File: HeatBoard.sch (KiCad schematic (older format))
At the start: 19 parts, among them J81 J8HeaderTurned, J82 J8Header, Q1 BC337, Q2 BC337

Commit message: First Final
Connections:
- net at Bu1.1 (V+), Co2.1 (P1), Co3.1 (P1)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: no longer R2.1 (P1)
- net at Co1.1 (P1), J81.1 (3.3V), J82.1 (3.3V)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: now also R2.1 (P1)
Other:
- moved on the sheet: Co2, Q1, R2, R3
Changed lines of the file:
@@
 L BC337 Q1
 U 1 1 5BE89444
-P 10050 3200
-F 0 "Q1" H 10250 3275 50  0000 L CNN
-F 1 "BC337" H 10250 3200 50  0000 L CNN
-F 2 "RasperryLib:BC337" H 10250 3125 50  0001 L CIN
-F 3 "" H 10050 3200 50  0001 L CNN
-	1    10050 3200
+P 10550 3200
+F 0 "Q1" H 10750 3275 50  0000 L CNN
+F 1 "BC337" H 10750 3200 50  0000 L CNN
+F 2 "RasperryLib:BC337" H 10750 3125 50  0001 L CIN
+F 3 "" H 10550 3200 50  0001 L CNN
+	1    10550 3200
 	1    0    0    -1
 $EndComp
@@
 L Conn_small1x3 Co2
 U 1 1 5BE8BABB
-P 6800 5950
-F 0 "Co2" H 6800 5700 60  0000 C CNN
-F 1 "DHT22" H 6800 6150 60  0000 C CNN
-F 2 "RasperryLib:Conn_Small1x3" H 6800 5950 60  0001 C CNN
-F 3 "" H 6800 5950 60  0001 C CNN
-	1    6800 5950
+P 7050 5950
+F 0 "Co2" H 7050 5700 60  0000 C CNN
+F 1 "DHT22" H 7050 6150 60  0000 C CNN
+F 2 "RasperryLib:Conn_Small1x3" H 7050 5950 60  0001 C CNN
+F 3 "" H 7050 5950 60  0001 C CNN
+	1    7050 5950
 	1    0    0    -1
 $EndComp
@@
 L Resistor R2
 U 1 1 5BE8E5B2
-P 6800 5200
-F 0 "R2" H 6800 5100 60  0000 C CNN
-F 1 "10k" H 6800 5300 60  0000 C CNN
-F 2 "RasperryLib:Resistor" H 6800 5200 60  0001 C CNN
-F 3 "" H 6800 5200 60  0001 C CNN
-	1    6800 5200
-	0    1    1    0
+P 6250 5950
+F 0 "R2" H 6250 5850 60  0000 C CNN
+F 1 "10k" H 6250 6050 60  0000 C CNN
+F 2 "RasperryLib:Resistor" H 6250 5950 60  0001 C CNN
+F 3 "" H 6250 5950 60  0001 C CNN
+	1    6250 5950
+	1    0    0    -1
 $EndComp
 $Comp
@@
 L Resistor R3
 U 1 1 5BE90BEE
-P 9650 3050
-F 0 "R3" H 9650 2950 60  0000 C CNN
-F 1 "1k" H 9650 3150 60  0000 C CNN
-F 2 "RasperryLib:Resistor" H 9650 3050 60  0001 C CNN
-F 3 "" H 9650 3050 60  0001 C CNN
-	1    9650 3050
-	0    1    1    0
+P 10100 3200
+F 0 "R3" H 10100 3100 60  0000 C CNN
+F 1 "1k" H 10100 3300 60  0000 C CNN
+F 2 "RasperryLib:Resistor" H 10100 3200 60  0001 C CNN
+F 3 "" H 10100 3200 60  0001 C CNN
+	1    10100 3200
+	1    0    0    -1
 $EndComp
 $Comp
@@
 	0    1    1    0
 $EndComp
+$Comp
+L Buzzer_2 Bu1
+U 1 1 5BE9F2D6
+P 8100 5050
+F 0 "Bu1" H 8100 4750 60  0000 C CNN
+F 1 "Buzzer_2" H 8100 5350 60  0000 C CNN
+F 2 "RasperryLib:Buzzer1x2" H 8100 4850 60  0001 C CNN
+F 3 "" H 8100 4850 60  0001 C CNN
+	1    8100 5050
+	1    0    0    -1
+$EndComp
+$Comp
+L BC337 Q2
+U 1 1 5BE9F3DC
+P 8000 5550
+F 0 "Q2" H 8200 5625 50  0000 L CNN
+F 1 "BC337" H 8200 5550 50  0000 L CNN
+F 2 "TO_SOT_Packages_THT:TO-92_Molded_Narrow" H 8200 5475 50  0001 L CIN
+F 3 "" H 8000 5550 50  0001 L CNN
+	1    8000 5550
+	1    0    0    -1
+$EndComp
+$Comp
+L Resistor R4
+U 1 1 5BE9F598
+P 7800 5250
+F 0 "R4" H 7800 5150 60  0000 C CNN
+F 1 "1k" H 7800 5350 60  0000 C CNN
+F 2 "RasperryLib:Resistor" H 7800 5250 60  0001 C CNN
+F 3 "" H 7800 5250 60  0001 C CNN
+	1    7800 5250
+	0    1    1    0
+$EndComp
 Wire Wire Line
 	4200 3850 4550 3850
@@
 	6150 5450 6150 5500
 Wire Wire Line
-	6550 5500 2600 5500
+	2600 5500 6550 5500
 Wire Wire Line
 	2600 5500 2600 5450
@@
 	9300 4250 7150 4250
 Wire Wire Line
-	7150 4250 7150 4050
-Wire Wire Line
-	7150 4050 6150 4050
+	7150 4050 7150 5850
+Wire Wire Line
+	6150 4050 7150 4050
 Wire Wire Line
 	9150 3550 9150 3850
 Connection ~ 10150 3750
-Wire Wire Line
-	10800 3000 10150 3000
 Connection ~ 10800 3750
 Wire Wire Line
-	10150 3400 9450 3400
-Wire Wire Line
 	9450 3400 9450 3850
 Wire Wire Line
-	6700 3850 6700 5850
-Connection ~ 6700 3850
-Wire Wire Line
-	6900 5850 6900 4050
-Connection ~ 6900 4050
+	6950 3850 6950 5850
+Connection ~ 6950 3850
+Connection ~ 7150 4050
 Wire Wire Line
 	7400 5850 7400 3850
@@
 Connection ~ 7600 4250
 Wire Wire Line
-	6800 5000 6700 5000
-Connection ~ 6700 5000
-Wire Wire Line
-	6800 5400 6800 5850
+	6800 5550 6800 5950
+Wire Wire Line
+	6800 5850 7050 5850
 Wire Wire Line
 	6150 5550 6800 5550
@@
 Connection ~ 4450 5650
 Wire Wire Line
-	4350 5950 4100 5950
+	4100 5950 6050 5950
 Connection ~ 4350 5950
 Wire Wire Line
 	4100 6350 4450 6350
 Connection ~ 4450 6350
-Wire Wire Line
-	6150 5750 6350 5750
-Wire Wire Line
-	9650 3250 9850 3250
-Wire Wire Line
-	9850 3250 9850 3200
 Connection ~ 9450 3550
-$Comp
-L Buzzer_2 Bu1
-U 1 1 5BE9F2D6
-P 8100 5050
-F 0 "Bu1" H 8100 4750 60  0000 C CNN
-F 1 "Buzzer_2" H 8100 5350 60  0000 C CNN
-F 2 "RasperryLib:Buzzer1x2" H 8100 4850 60  0001 C CNN
-F 3 "" H 8100 4850 60  0001 C CNN
-	1    8100 5050
-	1    0    0    -1
-$EndComp
 Wire Wire Line
 	8100 4850 8100 3850
 Connection ~ 8100 3850
-$Comp
-L BC337 Q2
-U 1 1 5BE9F3DC
-P 8000 5550
-F 0 "Q2" H 8200 5625 50  0000 L CNN
-F 1 "BC337" H 8200 5550 50  0000 L CNN
-F 2 "TO_SOT_Packages_THT:TO-92_Molded_Narrow" H 8200 5475 50  0001 L CIN
-F 3 "" H 8000 5550 50  0001 L CNN
-	1    8000 5550
-	1    0    0    -1
-$EndComp
 Wire Wire Line
 	8100 5250 8100 5350
@@
 	8350 5750 8350 4250
 Connection ~ 8350 4250
-$Comp
-L Resistor R4
-U 1 1 5BE9F598
-P 7800 5250
-F 0 "R4" H 7800 5150 60  0000 C CNN
-F 1 "1k" H 7800 5350 60  0000 C CNN
-F 2 "RasperryLib:Resistor" H 7800 5250 60  0001 C CNN
-F 3 "" H 7800 5250 60  0001 C CNN
-	1    7800 5250
-	0    1    1    0
-$EndComp
 Wire Wire Line
 	7800 5450 7800 5550
@@
 	6600 6250 6600 4050
 Connection ~ 6600 4050
-Wire Wire Line
-	6550 2850 6550 5500
-Wire Wire Line
-	6550 2850 9650 2850
 Connection ~ 6150 5500
+Connection ~ 6800 5850
+Wire Wire Line
+	6800 5950 6450 5950
+Connection ~ 7150 4250
+Wire Wire Line
+	6550 5500 6550 3200
+Wire Wire Line
+	6550 3200 9900 3200
+Wire Wire Line
+	10300 3200 10350 3200
+Wire Wire Line
+	10650 3400 9450 3400
+Wire Wire Line
+	10800 3000 10650 3000
 $EndSCHEMATC

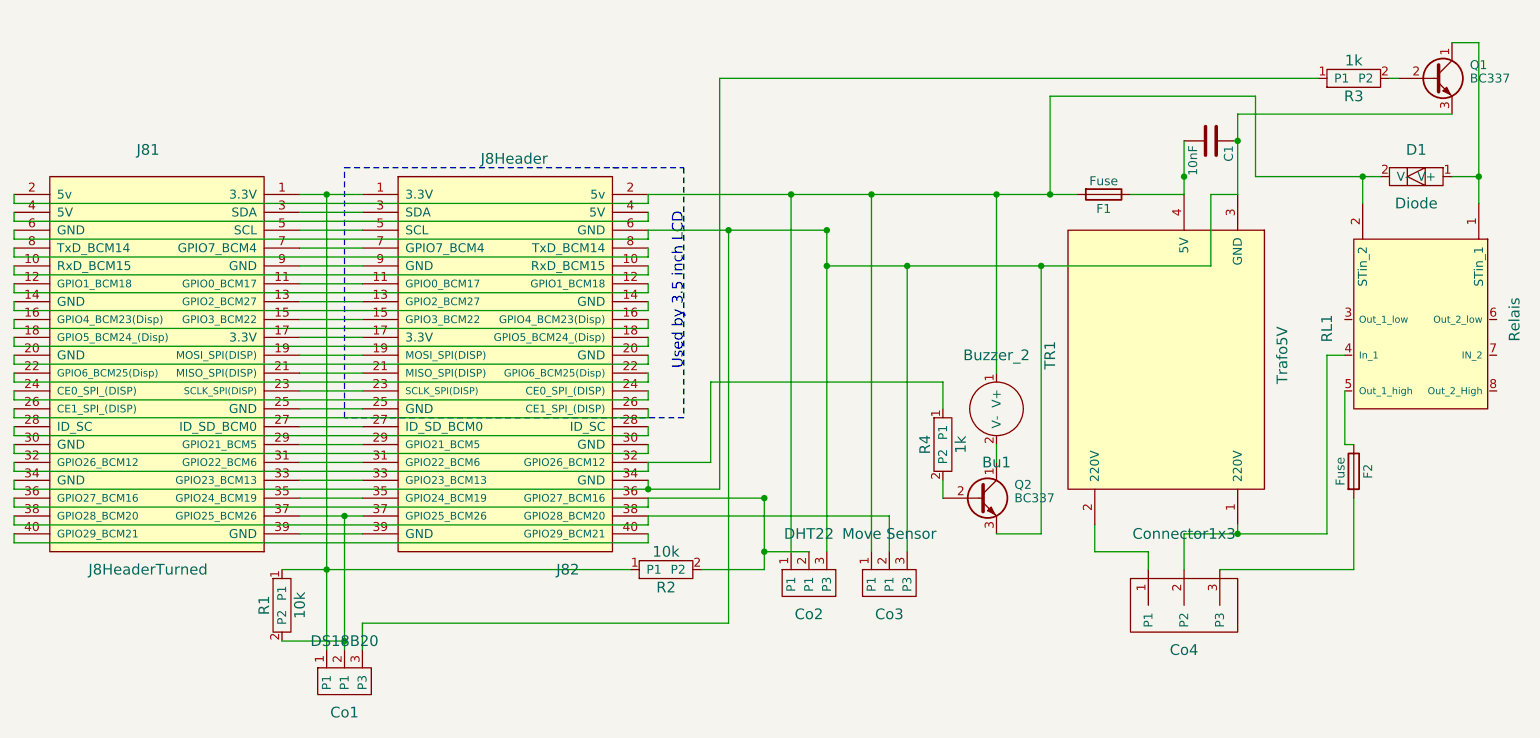
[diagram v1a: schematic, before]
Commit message: Raspi Connections move, GND Pin free now
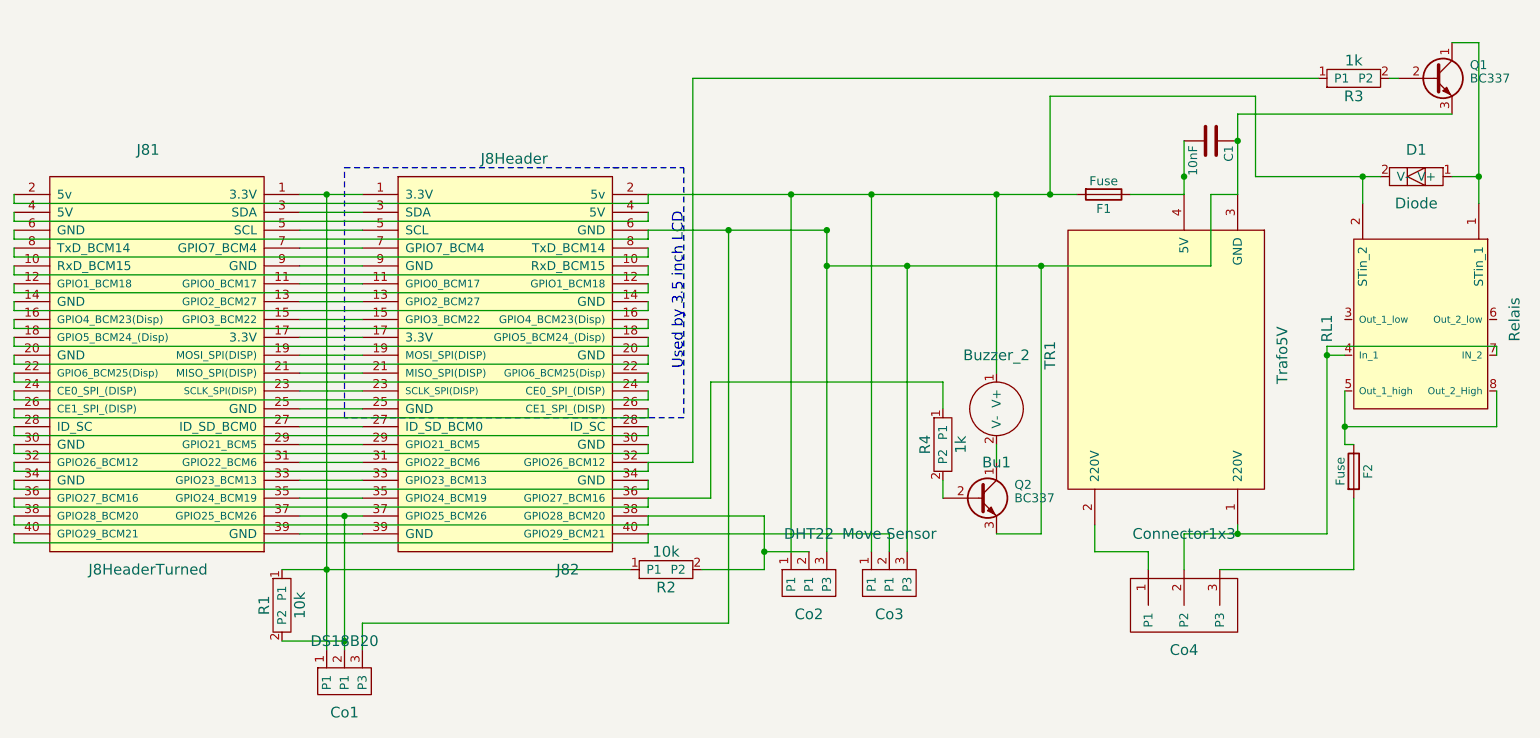
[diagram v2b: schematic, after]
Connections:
- net at Co4.2 (P2), RL1.4 (In_1), TR1.1 (220V): now also RL1.7 (IN_2)
- net at F2.1, RL1.5 (Out_1_high): now also RL1.8 (Out_2_High)
- net at J81.32 (GPIO26_BCM12), J82.32 (GPIO26_BCM12): now also R3.1 (P1); no longer R4.1 (P1)
- net at J81.34 (GND), J82.34 (GND): no longer R3.1 (P1)
- net at J81.36 (GPIO27_BCM16), J82.36 (GPIO27_BCM16): now also R4.1 (P1); no longer Co2.2 (P1), R2.2 (P2)
- net at J81.38 (GPIO28_BCM20), J82.38 (GPIO28_BCM20): now also Co2.2 (P1), R2.2 (P2); no longer Co3.2 (P1)
- net at J81.40 (GPIO29_BCM21), J82.40 (GPIO29_BCM21): now also Co3.2 (P1)
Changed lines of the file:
@@
 	6150 5450 6150 5500
 Wire Wire Line
-	2600 5500 6550 5500
+	6150 5500 2600 5500
 Wire Wire Line
 	2600 5500 2600 5450
@@
 	9150 5950 9150 5750
 Wire Wire Line
-	9150 5750 9950 5750
+	9950 5750 9150 5750
 Wire Wire Line
 	9450 5750 9450 5700
@@
 	10050 5250 10050 4950
 Wire Wire Line
-	9950 5750 9950 4750
+	9950 4700 9950 5750
 Wire Wire Line
 	9950 4750 10050 4750
@@
 Connection ~ 7600 4250
 Wire Wire Line
-	6800 5550 6800 5950
-Wire Wire Line
 	6800 5850 7050 5850
-Wire Wire Line
-	6150 5550 6800 5550
-Connection ~ 6800 5550
-Wire Wire Line
-	6150 5650 7500 5650
-Wire Wire Line
-	7500 5650 7500 5850
 Wire Wire Line
 	4350 3850 4350 6400
@@
 	7800 5450 7800 5550
 Wire Wire Line
-	6150 5350 6500 5350
-Wire Wire Line
-	6500 5350 6500 4900
+	6500 4900 6500 5550
 Wire Wire Line
 	6500 4900 7800 4900
@@
 	6600 6250 6600 4050
 Connection ~ 6600 4050
-Connection ~ 6150 5500
 Connection ~ 6800 5850
 Wire Wire Line
 	6800 5950 6450 5950
 Connection ~ 7150 4250
-Wire Wire Line
-	6550 5500 6550 3200
-Wire Wire Line
-	6550 3200 9900 3200
 Wire Wire Line
 	10300 3200 10350 3200
@@
 Wire Wire Line
 	10800 3000 10650 3000
+Wire Wire Line
+	6400 3200 6400 5350
+Wire Wire Line
+	6400 3200 9900 3200
+Wire Wire Line
+	6150 5750 7500 5750
+Wire Wire Line
+	7500 5750 7500 5850
+Wire Wire Line
+	6150 5650 6800 5650
+Wire Wire Line
+	6800 5650 6800 5950
+Wire Wire Line
+	6500 5550 6150 5550
+Wire Wire Line
+	6400 5350 6150 5350
+Wire Wire Line
+	10900 4950 10900 5150
+Wire Wire Line
+	10900 5150 10050 5150
+Connection ~ 10050 5150
+Wire Wire Line
+	9950 4700 10900 4700
+Wire Wire Line
+	10900 4700 10900 4750
+Connection ~ 9950 4750
 $EndSCHEMATC
